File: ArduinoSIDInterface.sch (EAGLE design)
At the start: 26 parts, among them IC1 74HC595N, IC2 74HC595N, T1 BC547

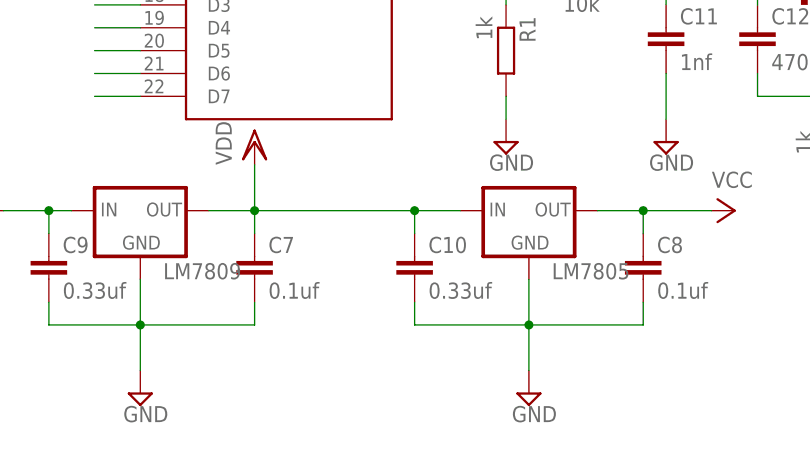
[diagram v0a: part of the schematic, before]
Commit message: Updated some packages on the schematic and slightly rearranged the board.
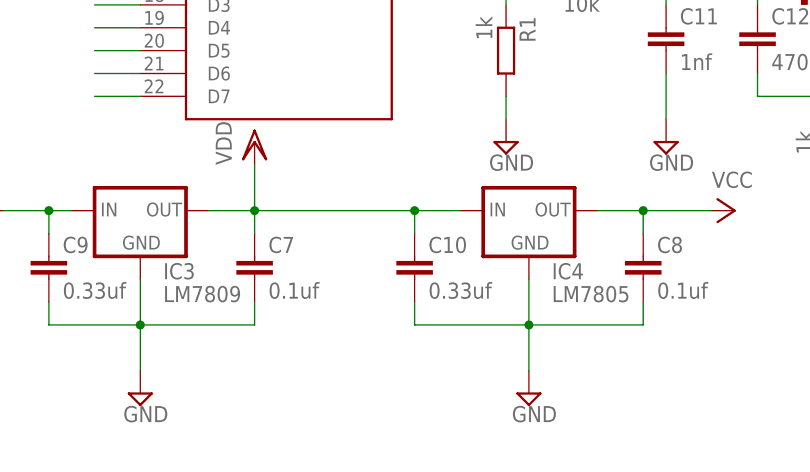
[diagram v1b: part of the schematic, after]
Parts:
- removed LM7805, LM7809: (no value), v-reg:78XXL
- added IC3: LM7809, v-reg:78XXS
- added IC4: LM7805, v-reg:78XXS
- C7, C8: device capacitor-wima:C7.5/3 -> capacitor-wima:C10/4
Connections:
- net GND: now also IC3.GND, IC4.GND; no longer LM7805.GND, LM7809.GND
- net V+: now also IC3.IN; no longer LM7809.IN
- net VCC: now also IC4.OUT; no longer LM7805.OUT
- net VDD: now also IC3.OUT, IC4.IN; no longer LM7805.IN, LM7809.OUT
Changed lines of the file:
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@@
 <grid distance="0.1" unitdist="inch" unit="inch" style="lines" multiple="1" display="no" altdistance="0.01" altunitdist="inch" altunit="inch"/>
 <layers>
-<layer number="1" name="Top" color="4" fill="1" visible="no" active="no"/>
-<layer number="16" name="Bottom" color="1" fill="1" visible="no" active="no"/>
-<layer number="17" name="Pads" color="2" fill="1" visible="no" active="no"/>
-<layer number="18" name="Vias" color="2" fill="1" visible="no" active="no"/>
-<layer number="19" name="Unrouted" color="6" fill="1" visible="no" active="no"/>
-<layer number="20" name="Dimension" color="15" fill="1" visible="no" active="no"/>
-<layer number="21" name="tPlace" color="7" fill="1" visible="no" active="no"/>
-<layer number="22" name="bPlace" color="7" fill="1" visible="no" active="no"/>
-<layer number="23" name="tOrigins" color="15" fill="1" visible="no" active="no"/>
-<layer number="24" name="bOrigins" color="15" fill="1" visible="no" active="no"/>
-<layer number="25" name="tNames" color="7" fill="1" visible="no" active="no"/>
-<layer number="26" name="bNames" color="7" fill="1" visible="no" active="no"/>
-<layer number="27" name="tValues" color="7" fill="1" visible="no" active="no"/>
-<layer number="28" name="bValues" color="7" fill="1" visible="no" active="no"/>
+<layer number="1" name="Top" color="4" fill="1" visible="yes" active="no"/>
+<layer number="16" name="Bottom" color="1" fill="1" visible="yes" active="no"/>
+<layer number="17" name="Pads" color="2" fill="1" visible="yes" active="no"/>
+<layer number="18" name="Vias" color="2" fill="1" visible="yes" active="no"/>
+<layer number="19" name="Unrouted" color="6" fill="1" visible="yes" active="no"/>
+<layer number="20" name="Dimension" color="15" fill="1" visible="yes" active="no"/>
+<layer number="21" name="tPlace" color="7" fill="1" visible="yes" active="no"/>
+<layer number="22" name="bPlace" color="7" fill="1" visible="yes" active="no"/>
+<layer number="23" name="tOrigins" color="15" fill="1" visible="yes" active="no"/>
+<layer number="24" name="bOrigins" color="15" fill="1" visible="yes" active="no"/>
+<layer number="25" name="tNames" color="7" fill="1" visible="yes" active="no"/>
+<layer number="26" name="bNames" color="7" fill="1" visible="yes" active="no"/>
+<layer number="27" name="tValues" color="7" fill="1" visible="yes" active="no"/>
+<layer number="28" name="bValues" color="7" fill="1" visible="yes" active="no"/>
 <layer number="29" name="tStop" color="7" fill="3" visible="no" active="no"/>
 <layer number="30" name="bStop" color="7" fill="6" visible="no" active="no"/>
@@
 <layer number="35" name="tGlue" color="7" fill="4" visible="no" active="no"/>
 <layer number="36" name="bGlue" color="7" fill="5" visible="no" active="no"/>
-<layer number="37" name="tTest" color="7" fill="1" visible="no" active="no"/>
-<layer number="38" name="bTest" color="7" fill="1" visible="no" active="no"/>
+<layer number="37" name="tTest" color="7" fill="1" visible="yes" active="no"/>
+<layer number="38" name="bTest" color="7" fill="1" visible="yes" active="no"/>
 <layer number="39" name="tKeepout" color="4" fill="11" visible="no" active="no"/>
 <layer number="40" name="bKeepout" color="1" fill="11" visible="no" active="no"/>
@@
 <layer number="44" name="Drills" color="7" fill="1" visible="no" active="no"/>
 <layer number="45" name="Holes" color="7" fill="1" visible="no" active="no"/>
-<layer number="46" name="Milling" color="3" fill="1" visible="no" active="no"/>
-<layer number="47" name="Measures" color="7" fill="1" visible="no" active="no"/>
-<layer number="48" name="Document" color="7" fill="1" visible="no" active="no"/>
-<layer number="49" name="Reference" color="7" fill="1" visible="no" active="no"/>
-<layer number="51" name="tDocu" color="7" fill="1" visible="no" active="no"/>
-<layer number="52" name="bDocu" color="7" fill="1" visible="no" active="no"/>
+<layer number="46" name="Milling" color="3" fill="1" visible="yes" active="no"/>
+<layer number="47" name="Measures" color="7" fill="1" visible="yes" active="no"/>
+<layer number="48" name="Document" color="7" fill="1" visible="yes" active="no"/>
+<layer number="49" name="Reference" color="7" fill="1" visible="yes" active="no"/>
+<layer number="51" name="tDocu" color="7" fill="1" visible="yes" active="no"/>
+<layer number="52" name="bDocu" color="7" fill="1" visible="yes" active="no"/>
 <layer number="91" name="Nets" color="2" fill="1" visible="yes" active="yes"/>
 <layer number="92" name="Busses" color="1" fill="1" visible="yes" active="yes"/>
@@
 <part name="C5" library="rcl" deviceset="C-EU" device="050-030X075" value="0.1uf"/>
 <part name="C6" library="rcl" deviceset="C-EU" device="050-030X075" value="0.1uf"/>
-<part name="LM7809" library="v-reg" deviceset="78XXL" device=""/>
-<part name="LM7805" library="v-reg" deviceset="78XXL" device=""/>
 <part name="C9" library="capacitor-wima" deviceset="C" device="15/5" value="0.33uf"/>
 <part name="C10" library="capacitor-wima" deviceset="C" device="15/5" value="0.33uf"/>
-<part name="C7" library="capacitor-wima" deviceset="C" device="7.5/3" value="0.1uf"/>
-<part name="C8" library="capacitor-wima" deviceset="C" device="7.5/3" value="0.1uf"/>
+<part name="C7" library="capacitor-wima" deviceset="C" device="10/4" value="0.1uf"/>
+<part name="C8" library="capacitor-wima" deviceset="C" device="10/4" value="0.1uf"/>
 <part name="SUPPLY10" library="supply2" deviceset="GND" device=""/>
 <part name="SUPPLY11" library="supply2" deviceset="GND" device=""/>
@@
 <part name="SUPPLY17" library="supply2" deviceset="GND" device=""/>
 <part name="P+4" library="supply1" deviceset="VCC" device=""/>
+<part name="IC3" library="v-reg" deviceset="78XXS" device="" value="LM7809"/>
+<part name="IC4" library="v-reg" deviceset="78XXS" device="" value="LM7805"/>
 </parts>
 <sheets>
@@
 <instance part="C5" gate="G$1" x="2.54" y="2.54"/>
 <instance part="C6" gate="G$1" x="-22.86" y="0"/>
-<instance part="LM7809" gate="A" x="45.72" y="15.24"/>
-<instance part="LM7805" gate="A" x="88.9" y="15.24"/>
 <instance part="C9" gate="G$1" x="35.56" y="10.16"/>
 <instance part="C10" gate="G$1" x="76.2" y="10.16"/>
@@
 <instance part="SUPPLY17" gate="GND" x="139.7" y="0"/>
 <instance part="P+4" gate="VCC" x="139.7" y="7.62"/>
+<instance part="IC3" gate="1" x="45.72" y="15.24"/>
+<instance part="IC4" gate="1" x="88.9" y="15.24"/>
 </instances>
 <busses>
@@
 <wire x1="45.72" y1="2.54" x2="58.42" y2="2.54" width="0.1524" layer="91"/>
 <wire x1="58.42" y1="2.54" x2="58.42" y2="5.08" width="0.1524" layer="91"/>
-<pinref part="LM7809" gate="A" pin="GND"/>
 <wire x1="45.72" y1="7.62" x2="45.72" y2="2.54" width="0.1524" layer="91"/>
 <junction x="45.72" y="2.54"/>
 <wire x1="45.72" y1="2.54" x2="45.72" y2="-2.54" width="0.1524" layer="91"/>
 <pinref part="SUPPLY10" gate="GND" pin="GND"/>
-</segment>
-<segment>
-<pinref part="LM7805" gate="A" pin="GND"/>
+<pinref part="IC3" gate="1" pin="GND"/>
+</segment>
+<segment>
 <wire x1="88.9" y1="7.62" x2="88.9" y2="2.54" width="0.1524" layer="91"/>
 <pinref part="C10" gate="G$1" pin="2"/>
@@
 <wire x1="88.9" y1="-2.54" x2="88.9" y2="2.54" width="0.1524" layer="91"/>
 <pinref part="SUPPLY11" gate="GND" pin="GND"/>
+<pinref part="IC4" gate="1" pin="GND"/>
 </segment>
 <segment>
@@
 </segment>
 <segment>
-<pinref part="LM7809" gate="A" pin="IN"/>
 <wire x1="38.1" y1="15.24" x2="35.56" y2="15.24" width="0.1524" layer="91"/>
 <wire x1="30.48" y1="15.24" x2="35.56" y2="15.24" width="0.1524" layer="91"/>
@@
 <junction x="35.56" y="15.24"/>
 <pinref part="SUPPLY12" gate="1" pin="V+"/>
+<pinref part="IC3" gate="1" pin="IN"/>
 </segment>
 </net>
@@
 </segment>
 <segment>
-<pinref part="LM7805" gate="A" pin="OUT"/>
 <wire x1="96.52" y1="15.24" x2="101.6" y2="15.24" width="0.1524" layer="91"/>
 <pinref part="C8" gate="G$1" pin="1"/>
@@
 <wire x1="101.6" y1="15.24" x2="109.22" y2="15.24" width="0.1524" layer="91"/>
 <junction x="101.6" y="15.24"/>
+<pinref part="IC4" gate="1" pin="OUT"/>
 </segment>
 <segment>
@@
 <pinref part="C10" gate="G$1" pin="1"/>
 <wire x1="76.2" y1="12.7" x2="76.2" y2="15.24" width="0.1524" layer="91"/>
-<pinref part="LM7805" gate="A" pin="IN"/>
 <wire x1="76.2" y1="15.24" x2="81.28" y2="15.24" width="0.1524" layer="91"/>
-<pinref part="LM7809" gate="A" pin="OUT"/>
 <wire x1="53.34" y1="15.24" x2="58.42" y2="15.24" width="0.1524" layer="91"/>
 <junction x="76.2" y="15.24"/>
@@
 <wire x1="58.42" y1="15.24" x2="58.42" y2="20.32" width="0.1524" layer="91"/>
 <pinref part="VDD1" gate="G$1" pin="VDD"/>
-</segment>
-<segment>
+<pinref part="IC3" gate="1" pin="OUT"/>
+<pinref part="IC4" gate="1" pin="IN"/>
+</segment>
+<segment>
